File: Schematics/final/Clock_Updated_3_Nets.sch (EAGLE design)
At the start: 53 parts, among them U1 ATMEGA328P

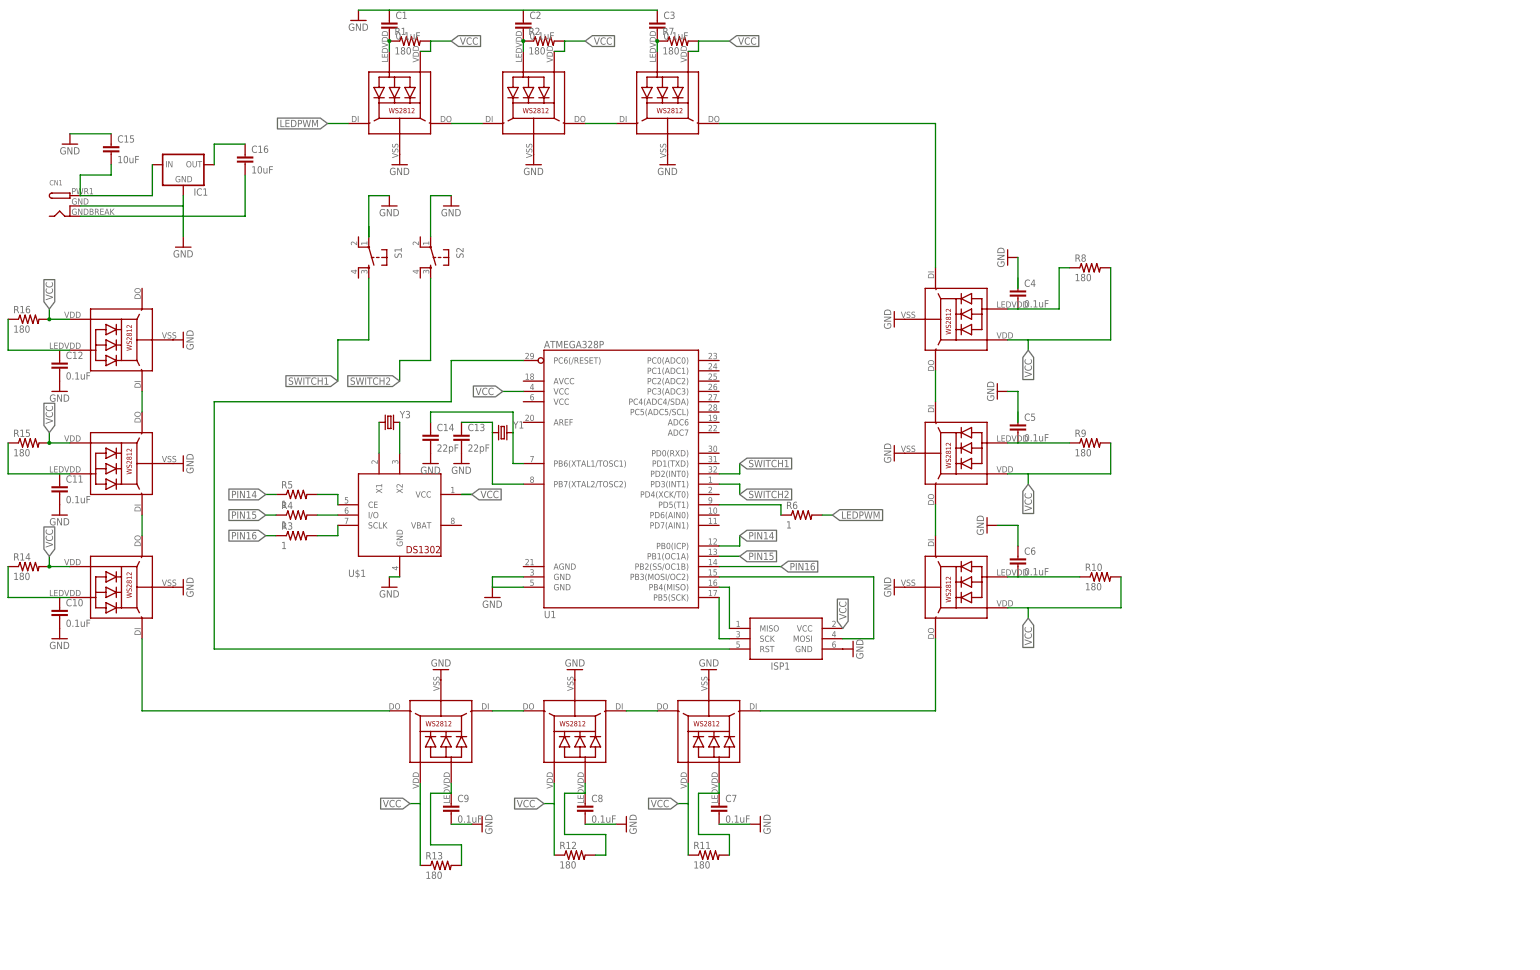
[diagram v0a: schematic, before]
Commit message: found out vdd and ledvdd were switched
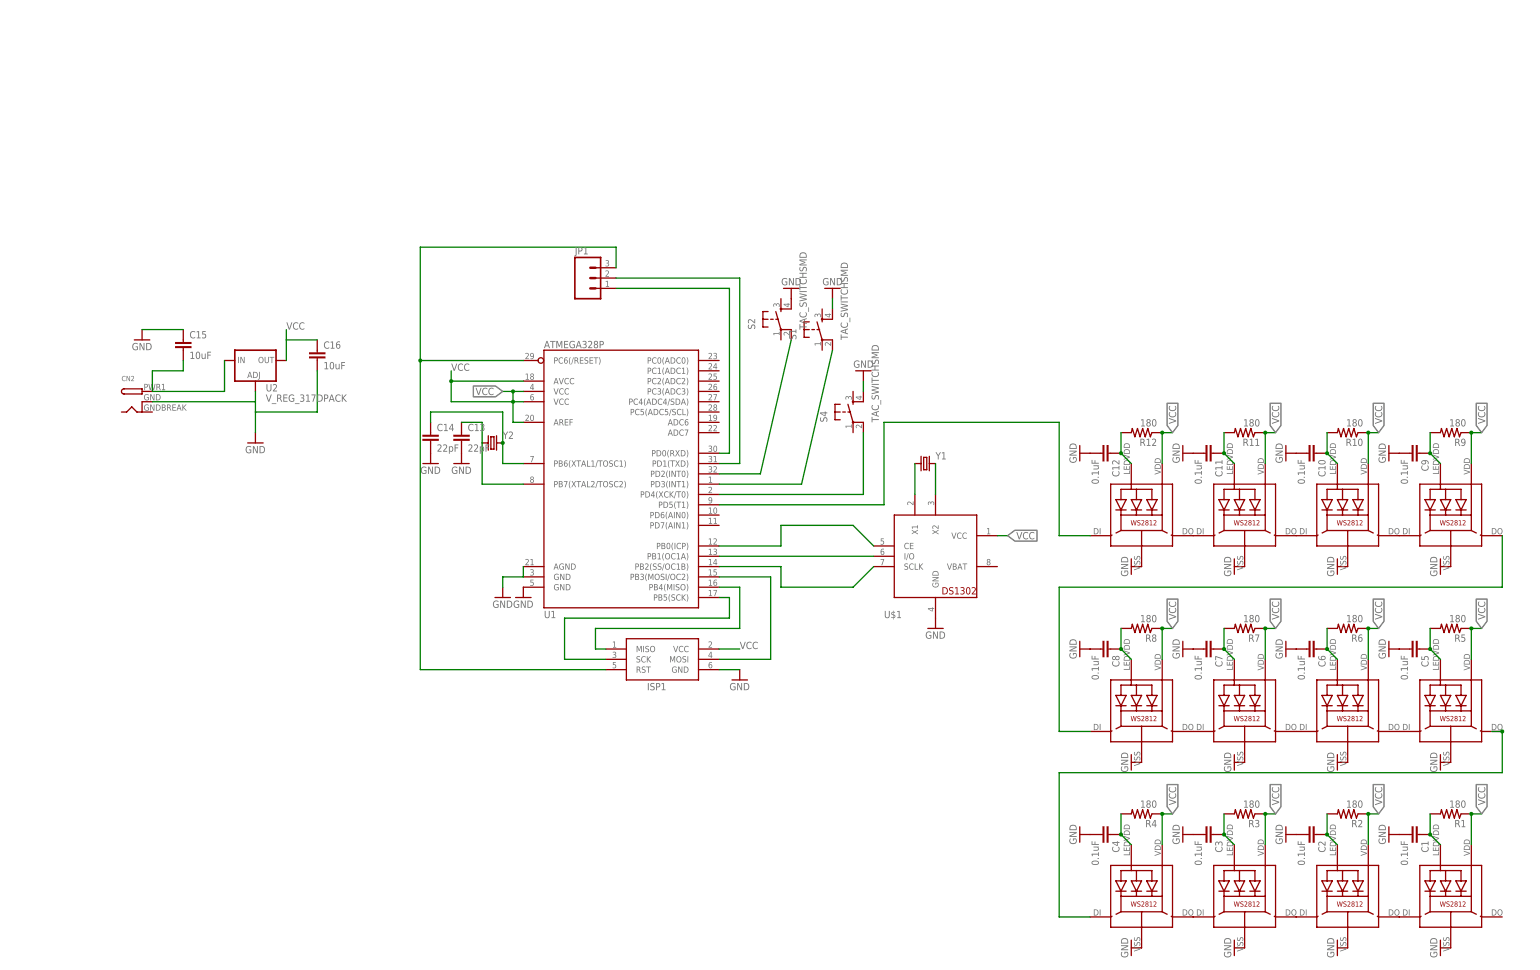
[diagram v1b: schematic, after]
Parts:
- removed CN1: (no value), adafruit:DCBARRELSMT
- removed IC1: (no value), SparkFun-PowerIC:V_REG_78XX-TO-220
- removed R13, R14, R15, R16: 180, SparkFun-Resistors:180OHM1/10W1%(0603)
- removed Y3: (no value), SparkFun-FreqCtrl:CRYSTAL32-SMD
- added CN2: (no value), adafruit:DCBARRELSMT
- added JP1: (no value), SparkFun-Connectors:M03JST-PTH-VERT
- added S4: TAC_SWITCHSMD, SparkFun-Electromechanical:TAC_SWITCHSMD
- added U2: V_REG_317DPACK, SparkFun-PowerIC:V_REG_317DPACK
- added Y2: (no value), SparkFun-FreqCtrl:CRYSTALSMD
- R3, R4, R5, R6: value 1 -> 180; device SparkFun-Resistors:1OHM1/10W1%(0603) -> SparkFun-Resistors:180OHM1/10W1%(0603)
- S1, S2: value (none) -> TAC_SWITCHSMD; device SparkFun-Electromechanical:TAC_SWITCHPTH -> SparkFun-Electromechanical:TAC_SWITCHSMD
- Y1: device SparkFun-FreqCtrl:CRYSTALSMD -> SparkFun-FreqCtrl:CRYSTALTC38H
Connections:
- removed net LEDPWM: LED1.DI, R6.2
- removed net N$1 (its old number): R6.1, U1.PD5(T1)
- removed net N$2 (its old number): C4.2, LED5.LEDVDD, R8.1
- removed net N$29: LED8.LEDVDD, R15.1
- removed net N$35: ISP1.RST, U1.PC6(/RESET)
- removed net N$39: C14.1, U1.PB6(XTAL1/TOSC1), Y1.2
- removed net PIN14: R5.1, U1.PB0(ICP)
- removed net PIN15: R4.1, U1.PB1(OC1A)
- removed net PIN16: R3.1, U1.PB2(SS/OC1B)
- removed net SWITCH1: S1.3, U1.PD2(INT0)
- removed net SWITCH2: S2.3, U1.PD3(INT1)
- new net N$33: U$1.SCLK, U1.PB2(SS/OC1B)
- new net N$40: LED2.DI, LED3.DO
- new net N$41: LED6.DI, LED7.DO
- new net N$42: LED10.DI, LED11.DO
- new net N$43: LED12.DI, U1.PD5(T1)
- new net N$44: C14.1, U1.PB6(XTAL1/TOSC1), Y2.2
- new net N$45: C15.2, CN2.PWR, U2.IN
- net GND: now also C1.2, C2.2, C3.2, C4.2, C5.2, C6.2, CN2.GNDBREAK, S1.4, S2.4, S4.4, U1.AGND, U2.ADJ; no longer C1.1, C3.1, C6.1, CN1.GND, CN1.GNDBREAK, IC1.GND, S1.1, S2.1
- net N$10: now also C3.1, LED3.LEDVDD, R3.2; no longer R4.2, U$1.I/O
- net N$11: now also C4.1, LED4.LEDVDD, R4.2; no longer R5.2, U$1.CE
- net N$12: now also LED3.DI, LED4.DO; no longer LED11.DO, LED4.DI
- net N$13: now also C5.1, LED5.LEDVDD, R5.2; no longer LED6.VDD, R9.2
- net N$14: now also C6.1, LED6.LEDVDD, R6.2; no longer LED12.DI, LED8.DO
- net N$15: now also LED5.DI, LED6.DO; no longer C7.1, LED9.LEDVDD, R11.2
- net N$16: now also C7.1, LED7.LEDVDD, R7.2; no longer LED6.DO, LED7.DI
- net N$17: now also C8.1, LED8.LEDVDD, R8.2; no longer LED3.DO, LED5.DI
- net N$18: now also LED7.DI, LED8.DO; no longer LED5.DO, LED6.DI
- net N$19: now also C9.1, LED9.LEDVDD, R9.2; no longer LED1.DO, LED2.DI
- net N$20: now also C10.1, LED10.LEDVDD, R10.2; no longer LED2.DO, LED3.DI
- net N$21: now also LED10.DO, LED9.DI; no longer C8.1, LED10.LEDVDD
- net N$22: now also C11.1, LED11.LEDVDD, R11.2; no longer LED4.DO, LED8.DI
- net N$23: now also C12.1, LED12.LEDVDD, R12.2; no longer C9.1, LED11.LEDVDD, R13.2
- net N$24: now also LED11.DI, LED12.DO; no longer LED12.LEDVDD, R16.1
- net N$25: now also LED4.DI, LED5.DO; no longer LED7.DO, LED9.DI
- net N$26: now also LED8.DI, LED9.DO; no longer R12.2
- net N$27: now also JP1.2, U1.PD1(TXD); no longer LED4.LEDVDD, R14.1
- net N$3: now also JP1.1, U1.PD0(RXD); no longer C5.2, LED6.LEDVDD, R9.1
- net N$30: now also S1.2, U1.PD3(INT1); no longer C1.2, LED1.LEDVDD, R1.1
- net N$31: now also U$1.I/O, U1.PB1(OC1A); no longer C2.2, LED2.LEDVDD, R2.1
- net N$32: now also U$1.CE, U1.PB0(ICP); no longer C3.2, LED3.LEDVDD, R7.1
- net N$36: now also ISP1.RST, JP1.3, U1.PC6(/RESET); no longer C15.2, CN1.PWR, IC1.IN
- net N$37: now also S4.2, U1.PD4(XCK/T0); no longer C16.1, IC1.OUT
- net N$38: now also Y2.1; no longer Y1.1
- net N$4: now also S2.2, U1.PD2(INT0); no longer C6.2, LED7.LEDVDD, R10.1
- net N$5: now also U$1.X2, Y1.2; no longer LED10.DI, LED9.DO
- net N$6: now also U$1.X1, Y1.1; no longer LED10.DO, LED11.DI
- net N$7: now also C1.1, LED1.LEDVDD, R1.2; no longer U$1.X2, Y3.2
- net N$8: now also C2.1, LED2.LEDVDD, R2.2; no longer U$1.X1, Y3.1
- net N$9: now also LED1.DI, LED2.DO; no longer R3.2, U$1.SCLK
- net VCC: now also C16.1, ISP1.VCC, LED6.VDD, R1.1, R10.1, R2.1, R3.1, R4.1, R5.1, R6.1, R7.1, R8.1, R9.1, U1.AREF, U1.AVCC, U1.VCC@2, U2.OUT; no longer R10.2, R13.1, R14.2, R15.2, R16.2, R8.2
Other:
- moved on the sheet: C1, C10, C11, C12, C15, C16, C2, C3, C4, C5, C6, C7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

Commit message: changed wires
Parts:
- removed C11, C12: 0.1uF, SparkFun-Capacitors:0.1UF-25V(+80/-20%)(0603)
- removed CN2: (no value), adafruit:DCBARRELSMT
- removed LED11, LED12: WS2812, adafruit:WS2812
- added C17, C18: 0.1uF, SparkFun-Capacitors:0.1UF-25V(+80/-20%)(0603)
- added LED13, LED14: WS2812, adafruit:WS2812
- added U$2: CUI_PJ-102A, con-dc-jack:CUI_PJ-102A
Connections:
- removed net N$22 (its old number): C11.1, LED11.LEDVDD, R11.2
- removed net N$23 (its old number): C12.1, LED12.LEDVDD, R12.2
- removed net N$24 (its old number): LED11.DI, LED12.DO
- new net N$12: LED3.LEDVDD, R5.2
- new net N$15: C5.1, LED5.VDD, R7.1
- new net N$18: LED6.LEDVDD, R8.2
- new net N$26: C7.1, LED7.VDD, R9.1
- new net N$29: C17.1, LED13.VDD, R1.1
- new net N$35: LED13.LEDVDD, R1.2
- new net N$39: C18.1, LED14.VDD, R2.1
- new net N$40: LED7.LEDVDD, R9.2
- new net N$41: C8.1, LED8.VDD, R10.1
- new net N$46: LED14.LEDVDD, R2.2
- new net N$47: C9.1, LED9.VDD, R11.1
- new net N$48: LED9.LEDVDD, R11.2
- new net N$49: C10.1, LED10.VDD, R12.1
- new net N$50: LED10.LEDVDD, R12.2
- new net N$56: C15.2, U$2.VDD
- new net N$9: C2.1, LED2.VDD, R4.1
- net GND: now also C17.2, C18.2, LED13.GND, LED14.GND; no longer C11.2, C12.2, CN2.GNDBREAK, LED11.GND, LED12.GND
- net N$10: now also LED2.LEDVDD, R4.2; no longer C3.1, LED3.LEDVDD, R3.2
- net N$11: now also C3.1, LED3.VDD, R5.1; no longer C4.1, LED4.LEDVDD, R4.2
- net N$13: now also C4.1, LED4.VDD, R6.1; no longer C5.1, LED5.LEDVDD, R5.2
- net N$14: now also LED4.LEDVDD; no longer C6.1, LED6.LEDVDD
- net N$16: now also LED5.LEDVDD; no longer C7.1, LED7.LEDVDD
- net N$17: now also C6.1, LED6.VDD, R8.1; no longer C8.1, LED8.LEDVDD, R8.2
- net N$19: now also LED13.DI, LED14.DO; no longer C9.1, LED9.LEDVDD, R9.2
- net N$20: now also LED1.DO, LED14.DI; no longer C10.1, LED10.LEDVDD, R10.2
- net N$42: now also LED8.LEDVDD, R10.2; no longer LED10.DI, LED11.DO
- net N$43: now also LED10.DI; no longer LED12.DI
- net N$45: now also U$2.VSS; no longer C15.2, CN2.PWR
- net N$7: now also LED1.VDD, R3.1; no longer LED1.LEDVDD, R1.2
- net N$8: now also LED1.LEDVDD, R3.2; no longer C2.1, LED2.LEDVDD, R2.2
- net VCC: no longer LED1.VDD, LED10.VDD, LED11.VDD, LED12.VDD, LED2.VDD, LED3.VDD, LED4.VDD, LED5.VDD, LED6.VDD, LED7.VDD, LED8.VDD, LED9.VDD, R1.1, R10.1, R11.1, R12.1, R2.1, R3.1, R4.1, R5.1, R6.1, R7.1, R8.1, R9.1
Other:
- moved on the sheet: C1, C10, C15, C2, C3, C4, C5, C6, C7, C8, C9, R1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
